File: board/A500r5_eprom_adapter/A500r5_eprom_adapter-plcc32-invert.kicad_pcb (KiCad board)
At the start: 2 copper layers, 40.6 x 54.6 mm, 9 parts, among them J2 A18 Selector, J3 A19 Selector, U1 27C400-A500, U2 27C080-L, U3 27C080-L

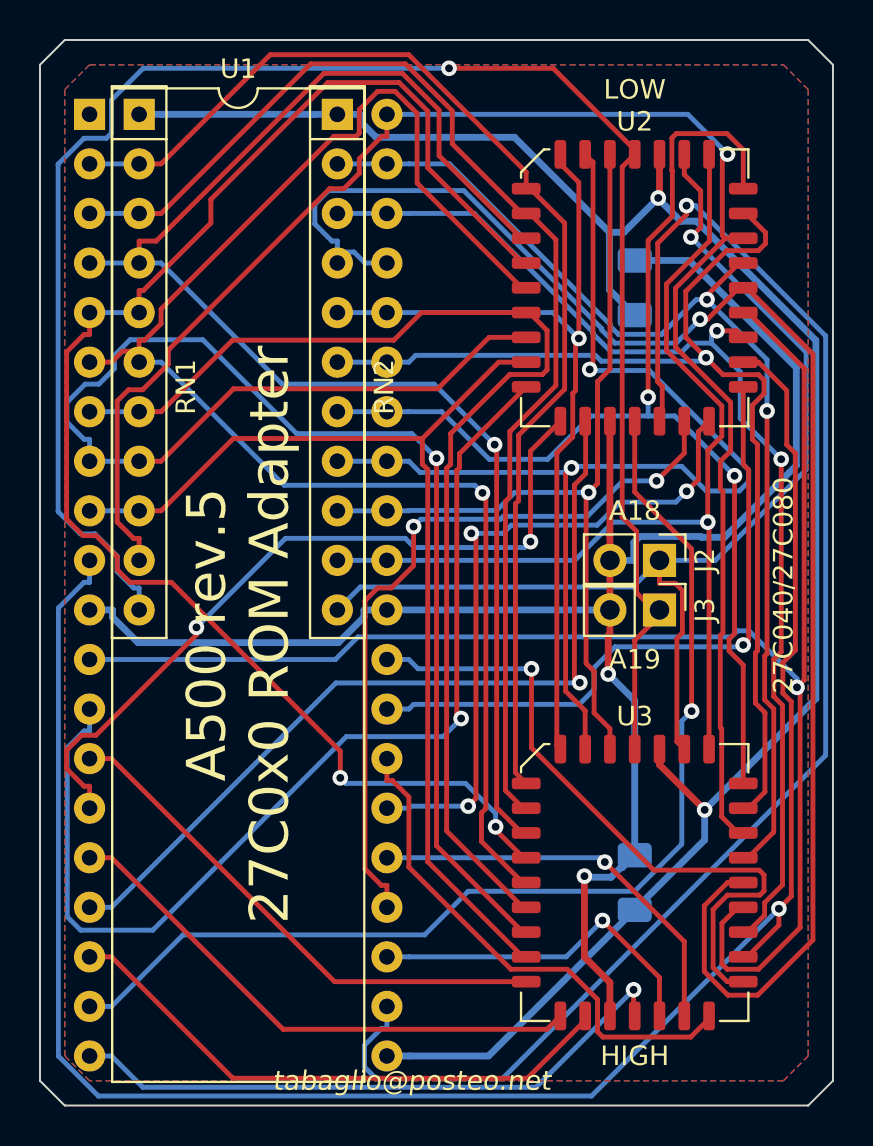
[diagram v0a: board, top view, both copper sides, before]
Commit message: Update the SMD variant
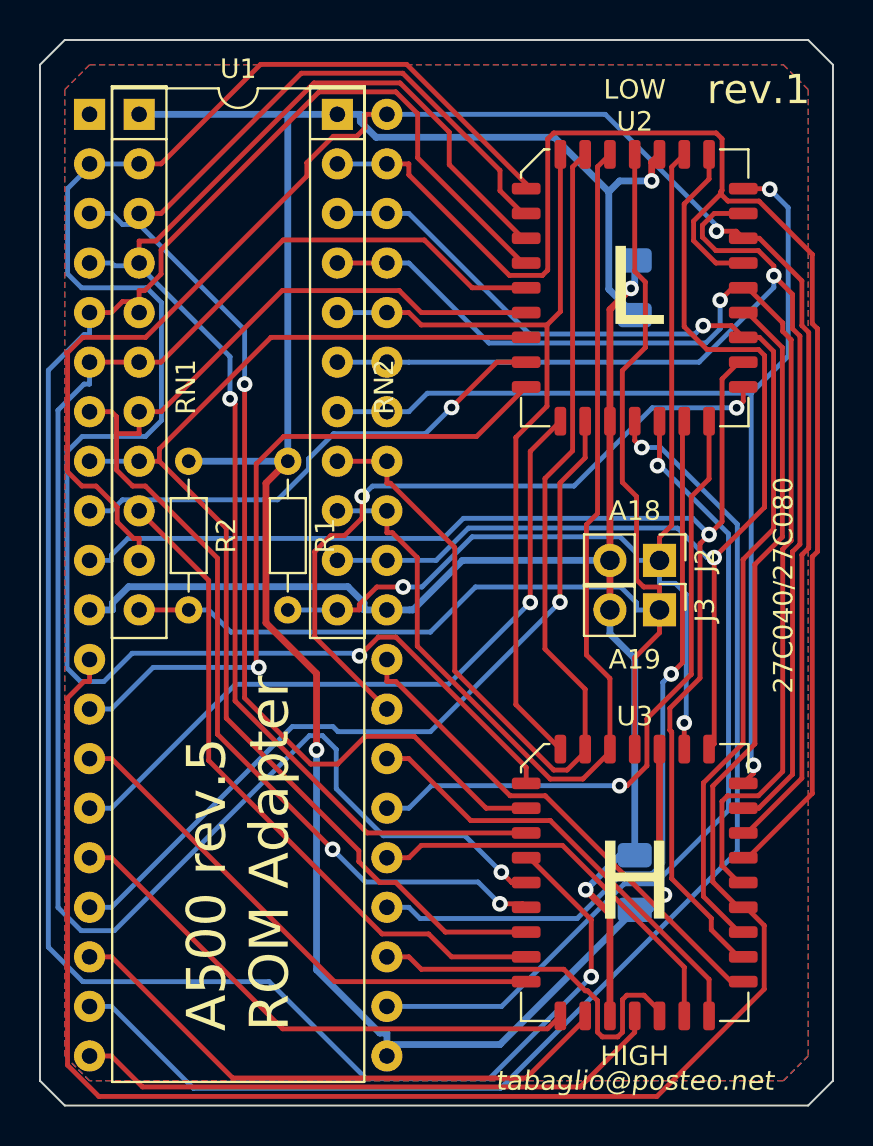
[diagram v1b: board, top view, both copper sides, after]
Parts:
- added R1: 4k7, Resistor_THT:R_Axial_DIN0204_L3.6mm_D1.6mm_P7.62mm_Horizontal, F.Cu at (120.7, 92.7)
- added R2: 4k7, Resistor_THT:R_Axial_DIN0204_L3.6mm_D1.6mm_P7.62mm_Horizontal, F.Cu at (115.6, 92.7)
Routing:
- net /~CE: track 101.6 -> 67.0 mm
- net /D4-L: track 77.7 -> 43.2 mm
- net /A19: track 92.1 -> 61.8 mm, vias 1 -> 0
- net /A4: track 77.8 -> 107.6 mm, vias 2 -> 1
- net /A7: track 60.7 -> 89.9 mm, vias 0 -> 1
- net /A11: track 81.2 -> 59.1 mm
- net /A9: track 57.0 -> 77.1 mm, vias 2 -> 0
- net /D0-L: track 54.8 -> 35.5 mm
- net GND: track 89.8 -> 70.9 mm
- net /~OE: track 80.0 -> 98.5 mm, vias 1 -> 0
- net /A1: track 78.1 -> 60.2 mm, vias 1 -> 0
- net VCC: track 101.2 -> 118.3 mm, vias 2 -> 3
- net /A6: track 62.5 -> 74.2 mm, vias 0 -> 1
- net /A16: track 44.8 -> 55.2 mm, vias 1 -> 0
- net /A3: track 78.0 -> 87.7 mm
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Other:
- board text added: "A500 rev.5 ROM Adapter"
- board text added: "H"
- board text added: "L"
- board text added: "rev.1"
- board text removed: "A500 rev.5 27C0x0 ROM Adapter"
